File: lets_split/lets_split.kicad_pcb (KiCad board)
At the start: 2 copper layers, 112 x 79 mm, 62 parts, among them J1 3PIN, J2 6PIN, J3 3PIN, SW1 SW_PUSH, SW10 SW_PUSH, SW11 SW_PUSH, SW12 SW_PUSH, SW13 SW_PUSH, SW14 SW_PUSH, SW15 SW_PUSH, SW16 SW_PUSH, SW17 SW_PUSH, SW18 SW_PUSH, SW19 SW_PUSH, SW2 SW_PUSH, SW20 SW_PUSH, SW21 SW_PUSH, SW22 SW_PUSH, SW23 SW_PUSH, SW24 SW_PUSH, SW3 SW_PUSH, SW4 SW_PUSH, SW5 SW_PUSH, SW6 SW_PUSH, SW7 SW_PUSH, SW8 SW_PUSH, SW9 SW_PUSH, U1 TEENSY2.0, U2 HOLE, U3 HOLE, U4 HOLE, U5 HOLE

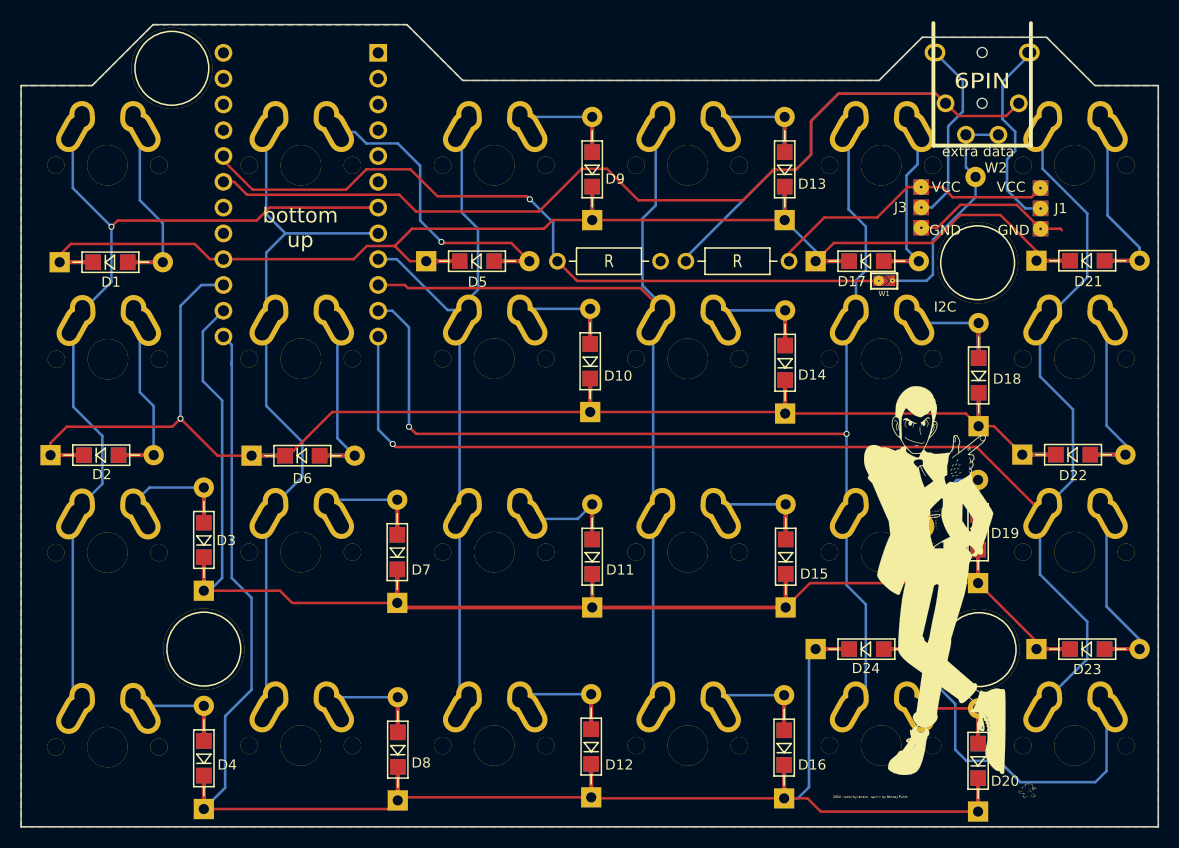
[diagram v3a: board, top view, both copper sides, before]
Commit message: Fix I2C related silks
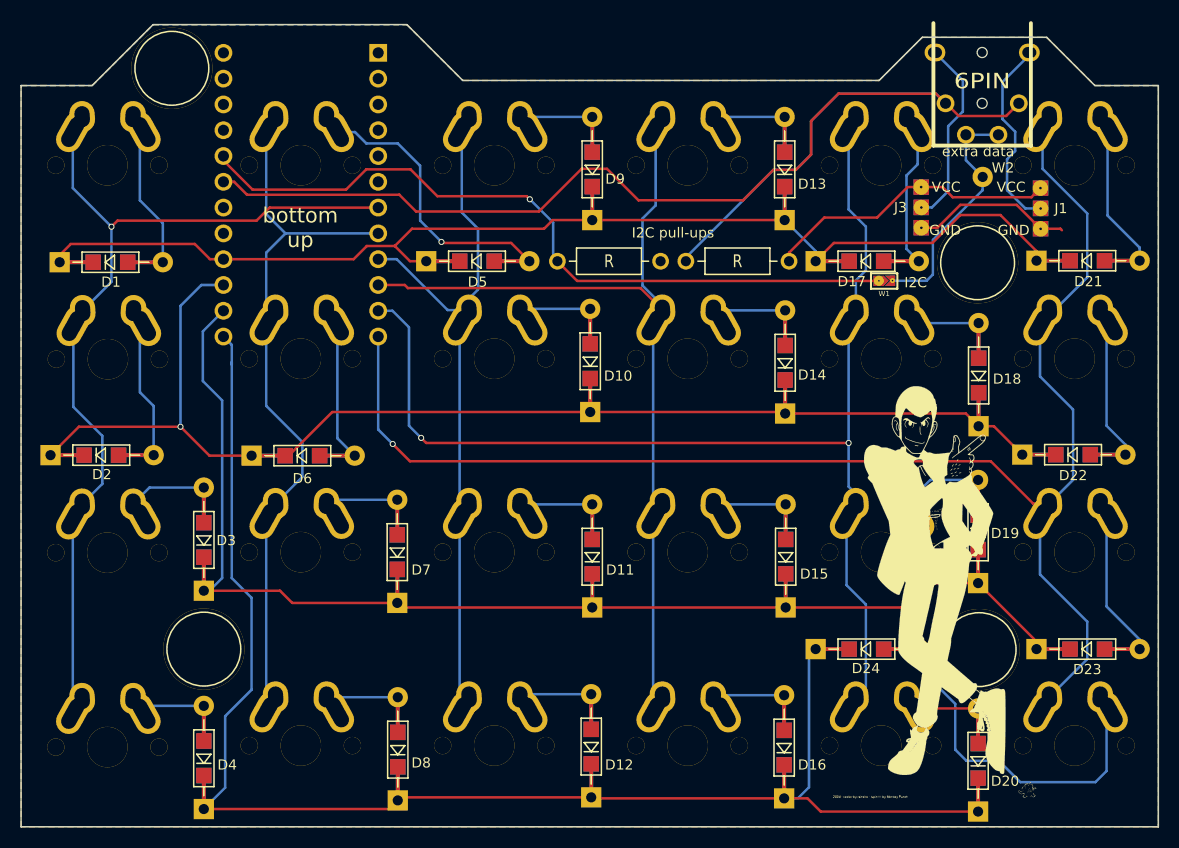
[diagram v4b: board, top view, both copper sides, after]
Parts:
- moved W2 0.70 mm to (131.7, 48.0)
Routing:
- net Net-(D11-Pad2): track 13.6 -> 15.9 mm
- net Net-(D19-Pad2): track 14.5 -> 16.8 mm
- net row1: track 159.1 -> 158.0 mm
- net xtradata: track 23.3 -> 23.9 mm
- net col4: track 112.3 -> 112.8 mm
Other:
- board text added: "I2C pull-ups"

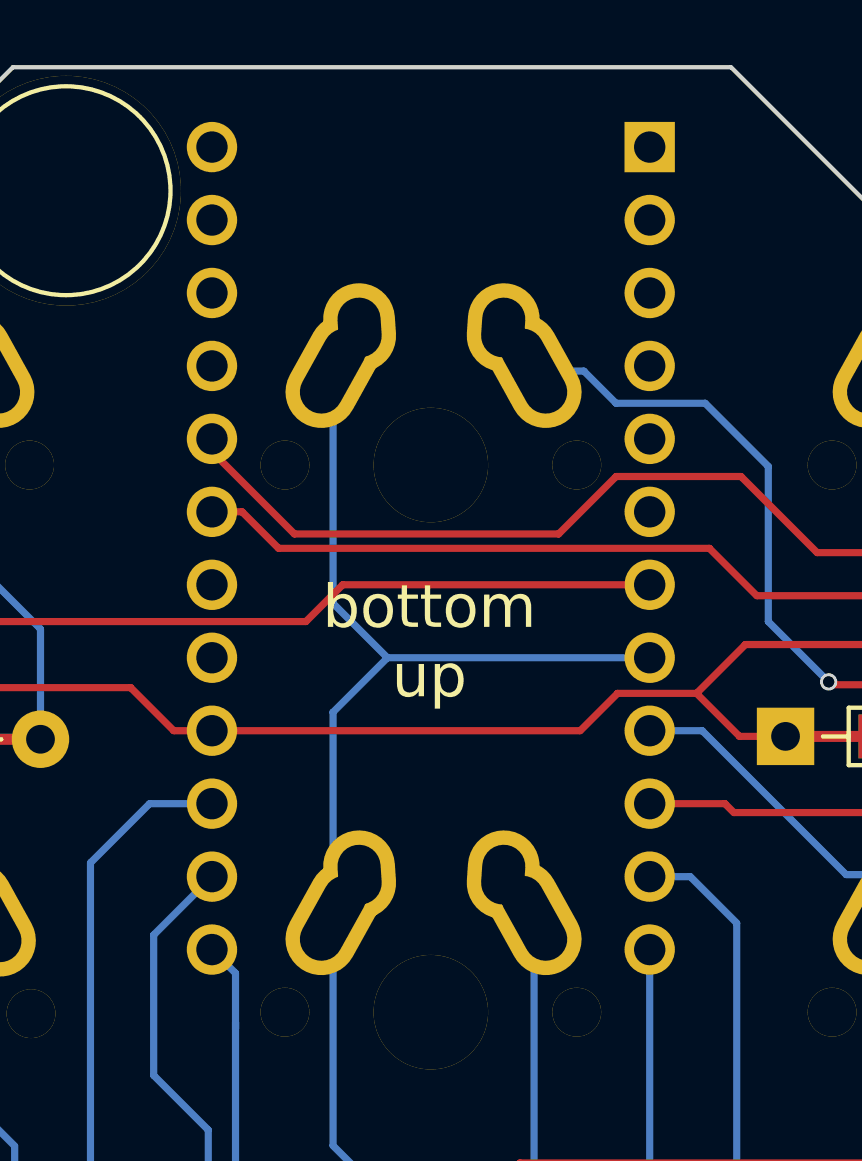
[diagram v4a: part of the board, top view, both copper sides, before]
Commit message: Replace Teensy 2.0 symbol with Pro Micro one
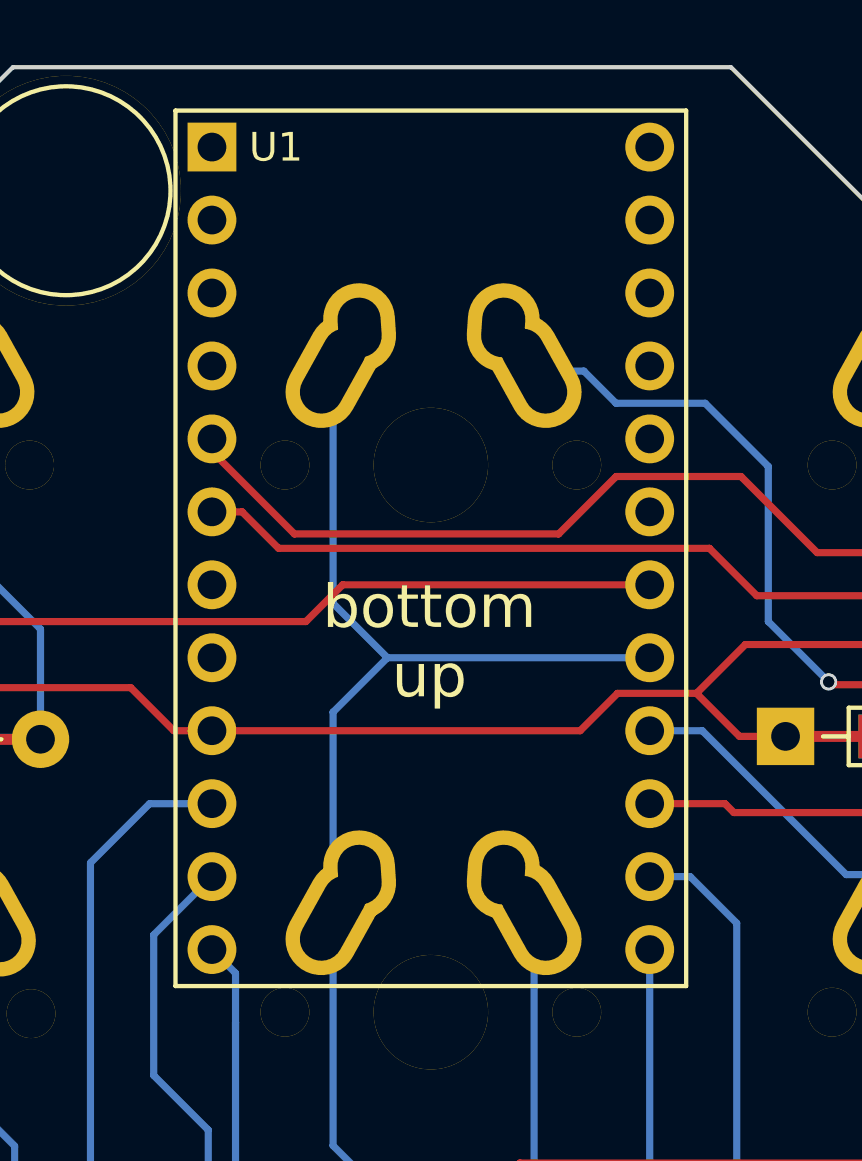
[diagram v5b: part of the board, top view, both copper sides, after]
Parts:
- U1: value TEENSY2.0 -> ProMicro; footprint footprint:TEENSY_2.0 -> local:ProMicro; moved to F.Cu
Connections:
- U1 pad 10: col3 -> row1
- U1 pad 11: col4 -> row2
- U1 pad 12: col5 -> row3
- U1 pad 18: row3 -> col0
- U1 pad 19: row2 -> (no net)
- U1 pad 2: GND -> (no net)
- U1 pad 20: row1 -> (no net)
- U1 pad 21: row0 -> VCC
- U1 pad 23: (no net) -> GND
- U1 pad 24: data -> (no net)
- U1 pad 3: (no net) -> GND
- U1 pad 4: VCC -> GND
- U1 pad 5: (no net) -> Net-(R1-Pad2)
- U1 pad 6: (no net) -> data
- U1 pad 7: col0 -> (no net)
- U1 pad 8: col1 -> (no net)
- U1 pad 9: col2 -> row0
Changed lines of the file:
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@@
   (general
     (thickness 1.6)
-    (drawings 31)
+    (drawings 35)
     (tracks 543)
     (zones 0)
@@
     (zone_45_only no)
     (trace_min 0.2)
-    (segment_width 0.2)
+    (segment_width 0.15)
     (edge_width 0.15)
     (via_size 0.6)
@@
     (add_net xtradata)
   )
+  (module local:ProMicro (layer F.Cu)
+    (at 64.55 49.75 270)
+    (fp_text reference U1 (at -13.9614 5.3934) (layer F.SilkS)
+      (effects (font (size 1 1) (thickness 0.15)))
+    )
+    (fp_text value ProMicro (at -13.97 -5.08 270) (layer F.Fab) hide
+      (effects (font (size 1 1) (thickness 0.15)))
+    )
+    (fp_line (start -15.24 8.89) (end -15.24 -8.89) (layer F.SilkS) (width 0.15))
+    (fp_line (start 15.24 8.89) (end -15.24 8.89) (layer F.SilkS) (width 0.15))
+    (fp_line (start 15.24 -8.89) (end 15.24 8.89) (layer F.SilkS) (width 0.15))
+    (fp_line (start -15.24 -8.89) (end 15.24 -8.89) (layer F.SilkS) (width 0.15))
+    (fp_text user "ProMicro 5V" (at -10.65 -0.15) (layer F.SilkS) hide
+      (effects (font (size 1.5 1.5) (thickness 0.3)))
+    )
+    (pad 24 thru_hole circle (at -13.97 -7.62 270) (size 1.7 1.7) (drill 1) (layers *.Cu *.Mask))
+    (pad 23 thru_hole circle (at -11.43 -7.62 270) (size 1.7 1.7) (drill 1) (layers *.Cu *.Mask)
+      (net 29 GND))
+    (pad 22 thru_hole circle (at -8.89 -7.62 270) (size 1.7 1.7) (drill 1) (layers *.Cu *.Mask))
+    (pad 21 thru_hole circle (at -6.35 -7.62 270) (size 1.7 1.7) (drill 1) (layers *.Cu *.Mask)
+      (net 31 VCC))
+    (pad 20 thru_hole circle (at -3.81 -7.62 270) (size 1.7 1.7) (drill 1) (layers *.Cu *.Mask))
+    (pad 19 thru_hole circle (at -1.27 -7.62 270) (size 1.7 1.7) (drill 1) (layers *.Cu *.Mask))
+    (pad 18 thru_hole circle (at 1.27 -7.62 270) (size 1.7 1.7) (drill 1) (layers *.Cu *.Mask)
+      (net 36 col0))
+    (pad 17 thru_hole circle (at 3.81 -7.62 270) (size 1.7 1.7) (drill 1) (layers *.Cu *.Mask)
+      (net 37 col1))
+    (pad 16 thru_hole circle (at 6.35 -7.62 270) (size 1.7 1.7) (drill 1) (layers *.Cu *.Mask)
+      (net 38 col2))
+    (pad 15 thru_hole circle (at 8.89 -7.62 270) (size 1.7 1.7) (drill 1) (layers *.Cu *.Mask)
+      (net 39 col3))
+    (pad 14 thru_hole circle (at 11.43 -7.62 270) (size 1.7 1.7) (drill 1) (layers *.Cu *.Mask)
+      (net 40 col4))
+    (pad 13 thru_hole circle (at 13.97 -7.62 270) (size 1.7 1.7) (drill 1) (layers *.Cu *.Mask)
+      (net 41 col5))
+    (pad 12 thru_hole circle (at 13.97 7.62 270) (size 1.7 1.7) (drill 1) (layers *.Cu *.Mask)
+      (net 8 row3))
+    (pad 11 thru_hole circle (at 11.43 7.62 270) (size 1.7 1.7) (drill 1) (layers *.Cu *.Mask)
+      (net 6 row2))
+    (pad 10 thru_hole circle (at 8.89 7.62 270) (size 1.7 1.7) (drill 1) (layers *.Cu *.Mask)
+      (net 4 row1))
+    (pad 9 thru_hole circle (at 6.35 7.62 270) (size 1.7 1.7) (drill 1) (layers *.Cu *.Mask)
+      (net 2 row0))
+    (pad 8 thru_hole circle (at 3.81 7.62 270) (size 1.7 1.7) (drill 1) (layers *.Cu *.Mask))
+    (pad 7 thru_hole circle (at 1.27 7.62 270) (size 1.7 1.7) (drill 1) (layers *.Cu *.Mask))
+    (pad 6 thru_hole circle (at -1.27 7.62 270) (size 1.7 1.7) (drill 1) (layers *.Cu *.Mask)
+      (net 32 data))
+    (pad 5 thru_hole circle (at -3.81 7.62 270) (size 1.7 1.7) (drill 1) (layers *.Cu *.Mask)
+      (net 35 "Net-(R1-Pad2)"))
+    (pad 4 thru_hole circle (at -6.35 7.62 270) (size 1.7 1.7) (drill 1) (layers *.Cu *.Mask)
+      (net 29 GND))
+    (pad 3 thru_hole circle (at -8.89 7.62 270) (size 1.7 1.7) (drill 1) (layers *.Cu *.Mask)
+      (net 29 GND))
+    (pad 2 thru_hole circle (at -11.43 7.62 270) (size 1.7 1.7) (drill 1) (layers *.Cu *.Mask))
+    (pad 1 thru_hole rect (at -13.97 7.62 270) (size 1.7 1.7) (drill 1) (layers *.Cu *.Mask))
+  )
   (module local:RESISTOR (layer B.Cu)
     (at 94.9 56.3 180)
@@
       (net 28 "Net-(D24-Pad2)"))
   )
-  (module footprint:TEENSY_2.0 (layer B.Cu)
-    (at 64.55 49.75 270)
-    (fp_text reference U1 (at 0 0 270) (layer B.SilkS) hide
-      (effects (font (size 3.048 2.54) (thickness 0.4572)) (justify mirror))
-    )
-    (fp_text value TEENSY2.0 (at 0 0 270) (layer B.SilkS) hide
-      (effects (font (size 3.048 2.54) (thickness 0.4572)) (justify mirror))
-    )
-    (fp_line (start -12.7 -6.35) (end -12.7 -8.89) (layer B.SilkS) (width 0.381))
-    (fp_line (start -15.24 -6.35) (end -12.7 -6.35) (layer B.SilkS) (width 0.381))
-    (fp_line (start 15.24 8.89) (end -15.24 8.89) (layer B.SilkS) (width 0.381))
-    (fp_line (start 15.24 -8.89) (end 15.24 8.89) (layer B.SilkS) (width 0.381))
-    (fp_line (start -15.24 -8.89) (end 15.24 -8.89) (layer B.SilkS) (width 0.381))
-    (fp_line (start -15.24 8.89) (end -15.24 -8.89) (layer B.SilkS) (width 0.381))
-    (fp_line (start 15.24 8.89) (end -15.24 8.89) (layer Cmts.User) (width 0.381))
-    (fp_line (start 15.24 -8.89) (end 15.24 8.89) (layer Cmts.User) (width 0.381))
-    (fp_line (start -15.24 -8.89) (end 15.24 -8.89) (layer Cmts.User) (width 0.381))
-    (fp_line (start -15.24 8.89) (end -15.24 -8.89) (layer Cmts.User) (width 0.381))
-    (fp_line (start 0 0) (end 0 0) (layer Dwgs.User) (width 0.0254))
-    (fp_line (start 15.24 8.89) (end -15.24 8.89) (layer Dwgs.User) (width 0.381))
-    (fp_line (start 15.24 -8.89) (end 15.24 8.89) (layer Dwgs.User) (width 0.381))
-    (fp_line (start -15.24 -8.89) (end 15.24 -8.89) (layer Dwgs.User) (width 0.381))
-    (fp_line (start -15.24 8.89) (end -15.24 -8.89) (layer Dwgs.User) (width 0.381))
-    (pad 26 thru_hole circle (at -6.35 7.62 270) (size 1.7526 1.7526) (drill 1.0922) (layers *.Cu *.SilkS *.Mask)
-      (net 29 GND))
-    (pad 25 thru_hole circle (at -3.81 7.62 270) (size 1.7526 1.7526) (drill 1.0922) (layers *.Cu *.SilkS *.Mask)
-      (net 35 "Net-(R1-Pad2)"))
-    (pad 29 thru_hole circle (at -13.97 7.62 270) (size 1.7526 1.7526) (drill 1.0922) (layers *.Cu *.SilkS *.Mask))
-    (pad 28 thru_hole circle (at -11.43 7.62 270) (size 1.7526 1.7526) (drill 1.0922) (layers *.Cu *.SilkS *.Mask))
-    (pad 27 thru_hole circle (at -8.89 7.62 270) (size 1.7526 1.7526) (drill 1.0922) (layers *.Cu *.SilkS *.Mask)
-      (net 29 GND))
-    (pad 24 thru_hole circle (at -1.27 7.62 270) (size 1.7526 1.7526) (drill 1.0922) (layers *.Cu *.SilkS *.Mask)
-      (net 32 data))
-    (pad 23 thru_hole circle (at 1.27 7.62 270) (size 1.7526 1.7526) (drill 1.0922) (layers *.Cu *.SilkS *.Mask))
-    (pad 22 thru_hole circle (at 3.81 7.62 270) (size 1.7526 1.7526) (drill 1.0922) (layers *.Cu *.SilkS *.Mask))
-    (pad 21 thru_hole circle (at 6.35 7.62 270) (size 1.7526 1.7526) (drill 1.0922) (layers *.Cu *.SilkS *.Mask)
-      (net 2 row0))
-    (pad 20 thru_hole circle (at 8.89 7.62 270) (size 1.7526 1.7526) (drill 1.0922) (layers *.Cu *.SilkS *.Mask)
-      (net 4 row1))
-    (pad 19 thru_hole circle (at 11.43 7.62 270) (size 1.7526 1.7526) (drill 1.0922) (layers *.Cu *.SilkS *.Mask)
-      (net 6 row2))
-    (pad 18 thru_hole circle (at 13.97 7.62 270) (size 1.7526 1.7526) (drill 1.0922) (layers *.Cu *.SilkS *.Mask)
-      (net 8 row3))
-    (pad 12 thru_hole circle (at 13.97 -7.62 270) (size 1.7526 1.7526) (drill 1.0922) (layers *.Cu *.SilkS *.Mask)
-      (net 41 col5))
-    (pad 11 thru_hole circle (at 11.43 -7.62 270) (size 1.7526 1.7526) (drill 1.0922) (layers *.Cu *.SilkS *.Mask)
-      (net 40 col4))
-    (pad 10 thru_hole circle (at 8.89 -7.62 270) (size 1.7526 1.7526) (drill 1.0922) (layers *.Cu *.SilkS *.Mask)
-      (net 39 col3))
-    (pad 9 thru_hole circle (at 6.35 -7.62 270) (size 1.7526 1.7526) (drill 1.0922) (layers *.Cu *.SilkS *.Mask)
-      (net 38 col2))
-    (pad 8 thru_hole circle (at 3.81 -7.62 270) (size 1.7526 1.7526) (drill 1.0922) (layers *.Cu *.SilkS *.Mask)
-      (net 37 col1))
-    (pad 7 thru_hole circle (at 1.27 -7.62 270) (size 1.7526 1.7526) (drill 1.0922) (layers *.Cu *.SilkS *.Mask)
-      (net 36 col0))
-    (pad 6 thru_hole circle (at -1.27 -7.62 270) (size 1.7526 1.7526) (drill 1.0922) (layers *.Cu *.SilkS *.Mask))
-    (pad 5 thru_hole circle (at -3.81 -7.62 270) (size 1.7526 1.7526) (drill 1.0922) (layers *.Cu *.SilkS *.Mask))
-    (pad 4 thru_hole circle (at -6.35 -7.62 270) (size 1.7526 1.7526) (drill 1.0922) (layers *.Cu *.SilkS *.Mask)
-      (net 31 VCC))
-    (pad 3 thru_hole circle (at -8.89 -7.62 270) (size 1.7526 1.7526) (drill 1.0922) (layers *.Cu *.SilkS *.Mask))
-    (pad 2 thru_hole circle (at -11.43 -7.62 270) (size 1.7526 1.7526) (drill 1.0922) (layers *.Cu *.SilkS *.Mask)
-      (net 29 GND))
-    (pad 1 thru_hole rect (at -13.97 -7.62 270) (size 1.7526 1.7526) (drill 1.0922) (layers *.Cu *.SilkS *.Mask))
-  )
   (module Wire_Pads:SolderWirePad_single_2mmDrill (layer F.Cu)
     (at 131.7 48)
@@
     (pad "" thru_hole circle (at -1.65 -0.7) (size 8 8) (drill 8) (layers *.Cu *.Mask F.SilkS))
   )
+  (gr_line (start 55.6641 34.5059) (end 73.4441 34.5059) (angle 90) (layer B.SilkS) (width 0.15))
+  (gr_line (start 55.6641 64.9859) (end 55.6641 34.5059) (angle 90) (layer B.SilkS) (width 0.15))
+  (gr_line (start 73.4441 64.9859) (end 55.6641 64.9859) (angle 90) (layer B.SilkS) (width 0.15))
+  (gr_line (start 73.4441 34.5059) (end 73.4441 64.9859) (angle 90) (layer B.SilkS) (width 0.15))
   (gr_text "I2C pull-ups" (at 101.1 53.5) (layer B.SilkS)
     (effects (font (size 1 1) (thickness 0.25)) (justify mirror))
